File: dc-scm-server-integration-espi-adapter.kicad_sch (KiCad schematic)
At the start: 0 parts

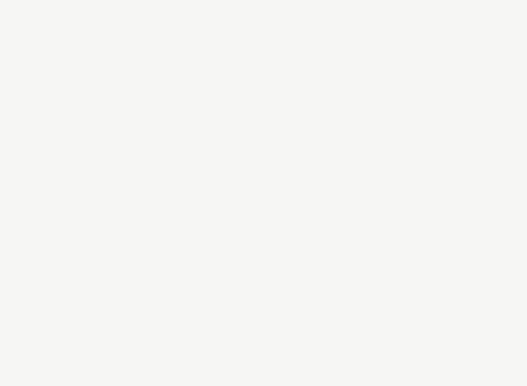
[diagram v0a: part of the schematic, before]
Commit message: [#103224] Add JTAG connector, add 2nd QSPI flash in co-layout, add Antmicro and OSH logos
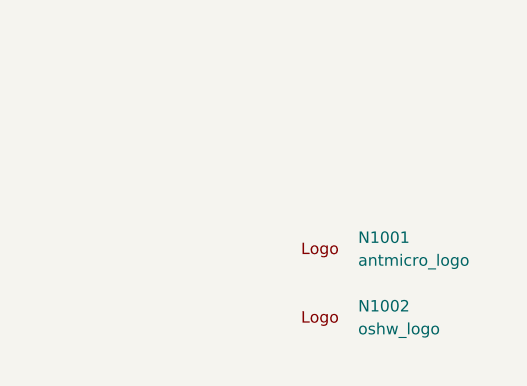
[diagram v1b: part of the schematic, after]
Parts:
- added N1001: antmicro_logo, antmicro-footprints:antmicro-logo, symbol Antmicro Symbols:antmicro_logo
- added N1002: oshw_logo, antmicro-footprints:oshw-logo, symbol Antmicro Symbols:oshw_logo

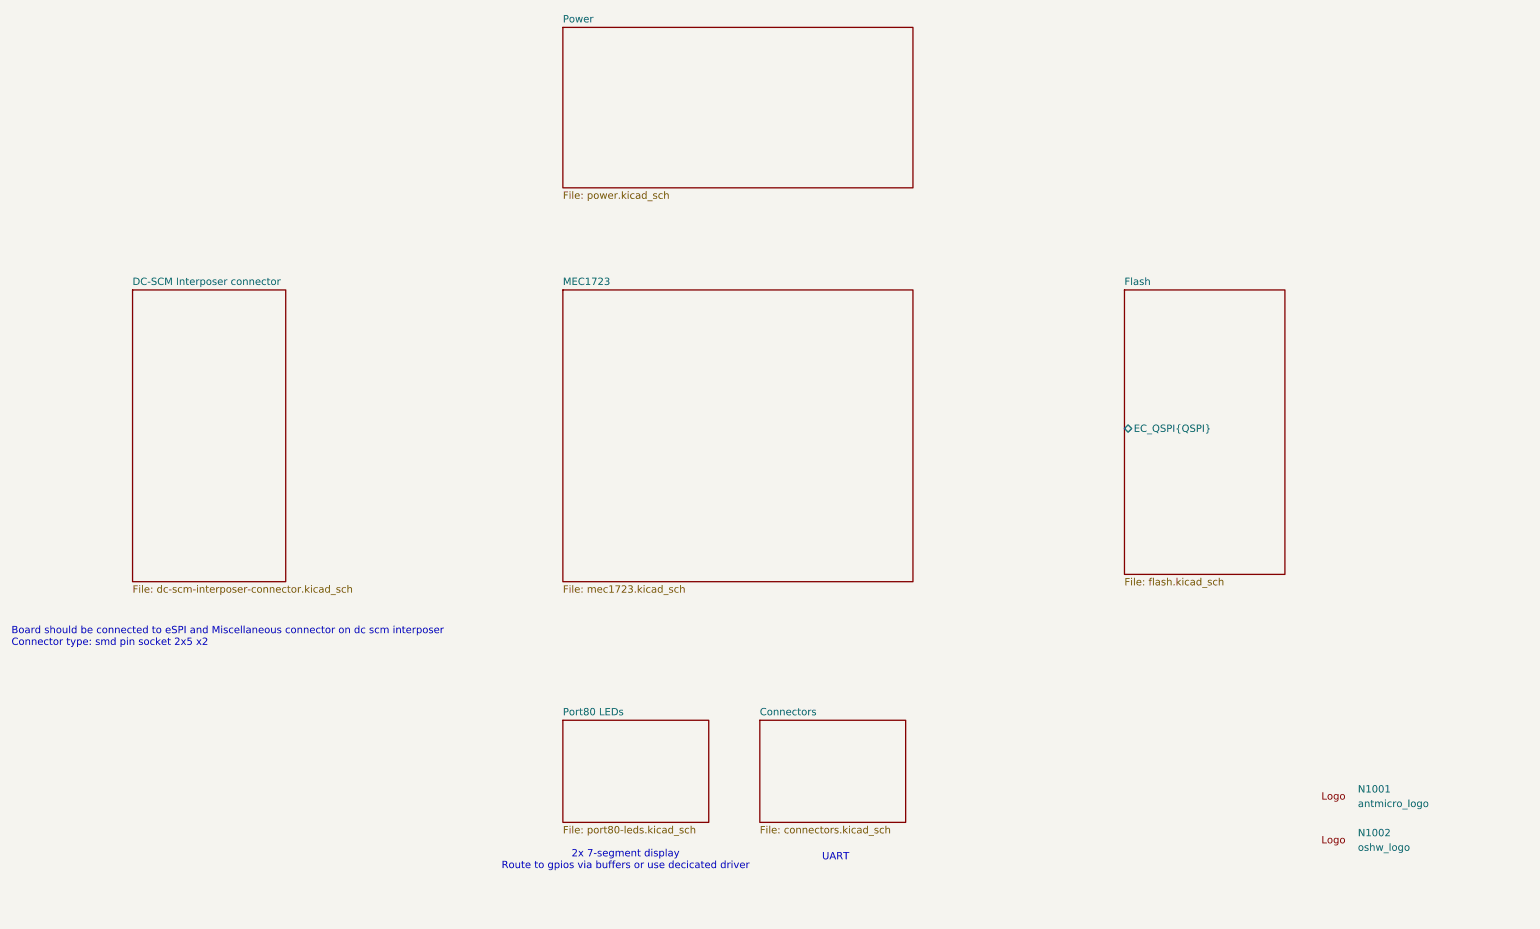
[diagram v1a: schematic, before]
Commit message: [#103224] Add MEC1723 IC, JTAG connections, eSPI connections, QSPI connections, fix typo in UART
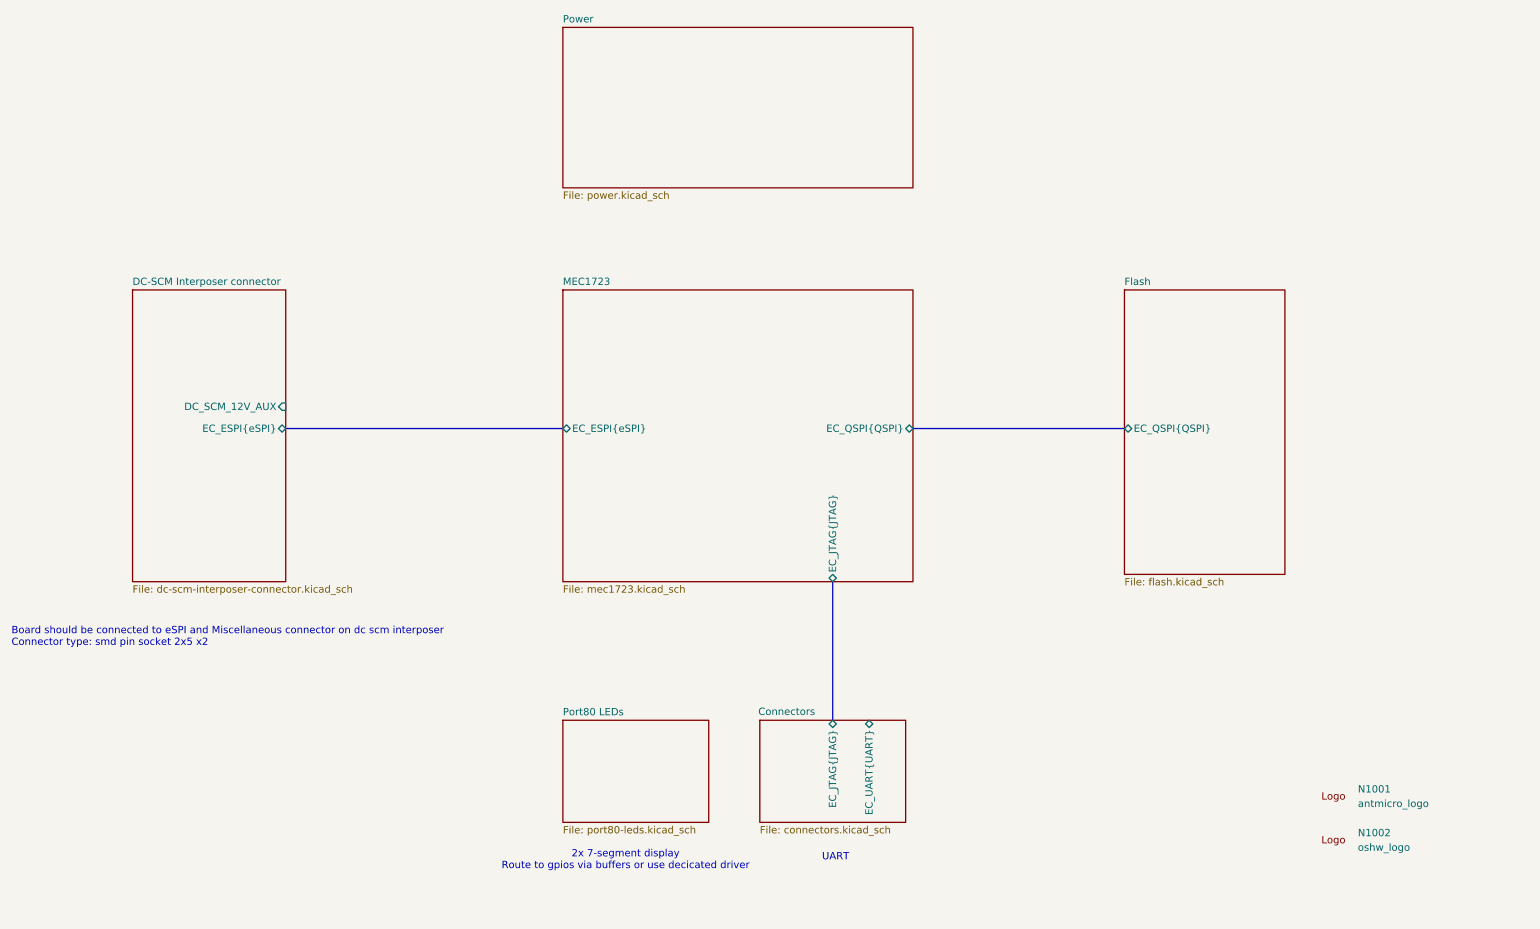
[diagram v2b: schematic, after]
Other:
- sheet Connectors ports: added EC_JTAG{JTAG}, EC_UART{UART}; removed none
- sheet DC-SCM Interposer connector ports: added DC_SCM_12V_AUX, EC_ESPI{eSPI}; removed none
- sheet MEC1723 ports: added EC_ESPI{eSPI}, EC_JTAG{JTAG}, EC_QSPI{QSPI}; removed none
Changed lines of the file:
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@@
+		)
+	)
+	(bus
+		(pts
+			(xy 179.07 90.17) (xy 215.9 90.17)
+		)
+		(stroke
+			(width 0)
+			(type default)
+		)
+	)
+	(bus
+		(pts
+			(xy 165.1 116.84) (xy 165.1 140.97)
+		)
+		(stroke
+			(width 0)
+			(type default)
+		)
+	)
+	(bus
+		(pts
+			(xy 69.85 90.17) (xy 118.11 90.17)
+		)
+		(stroke
+			(width 0)
+			(type default)
 		)
 	)
@@
 		(on_board yes)
 		(dnp no)
-		(fields_autoplaced yes)
 		(stroke
 			(width 0.1524)
@@
 		)
 		(property "Sheetname" "Connectors"
-			(at 152.4 140.2584 0)
+			(at 152.146 140.208 0)
 			(show_name no)
 			(do_not_autoplace no)
@@
 				)
 				(justify left top)
+			)
+		)
+		(pin "EC_JTAG{JTAG}" bidirectional
+			(at 165.1 140.97 90)
+			(effects
+				(font
+					(size 1.27 1.27)
+				)
+				(justify right)
+			)
+		)
+		(pin "EC_UART{UART}" bidirectional
+			(at 171.45 140.97 90)
+			(effects
+				(font
+					(size 1.27 1.27)
+				)
+				(justify right)
 			)
 		)
@@
 			)
 		)
+		(pin "EC_ESPI{eSPI}" bidirectional
+			(at 118.11 90.17 180)
+			(effects
+				(font
+					(size 1.27 1.27)
+				)
+				(justify left)
+			)
+		)
+		(pin "EC_JTAG{JTAG}" bidirectional
+			(at 165.1 116.84 270)
+			(effects
+				(font
+					(size 1.27 1.27)
+				)
+				(justify left)
+			)
+		)
+		(pin "EC_QSPI{QSPI}" bidirectional
+			(at 179.07 90.17 0)
+			(effects
+				(font
+					(size 1.27 1.27)
+				)
+				(justify right)
+			)
+		)
 		(instances
 			(project "dc-scm-server-integration-espi-adapter"
@@
 			)
 		)
+		(pin "DC_SCM_12V_AUX" input
+			(at 69.85 86.36 0)
+			(effects
+				(font
+					(size 1.27 1.27)
+				)
+				(justify right)
+			)
+		)
+		(pin "EC_ESPI{eSPI}" bidirectional
+			(at 69.85 90.17 0)
+			(effects
+				(font
+					(size 1.27 1.27)
+				)
+				(justify right)
+			)
+		)

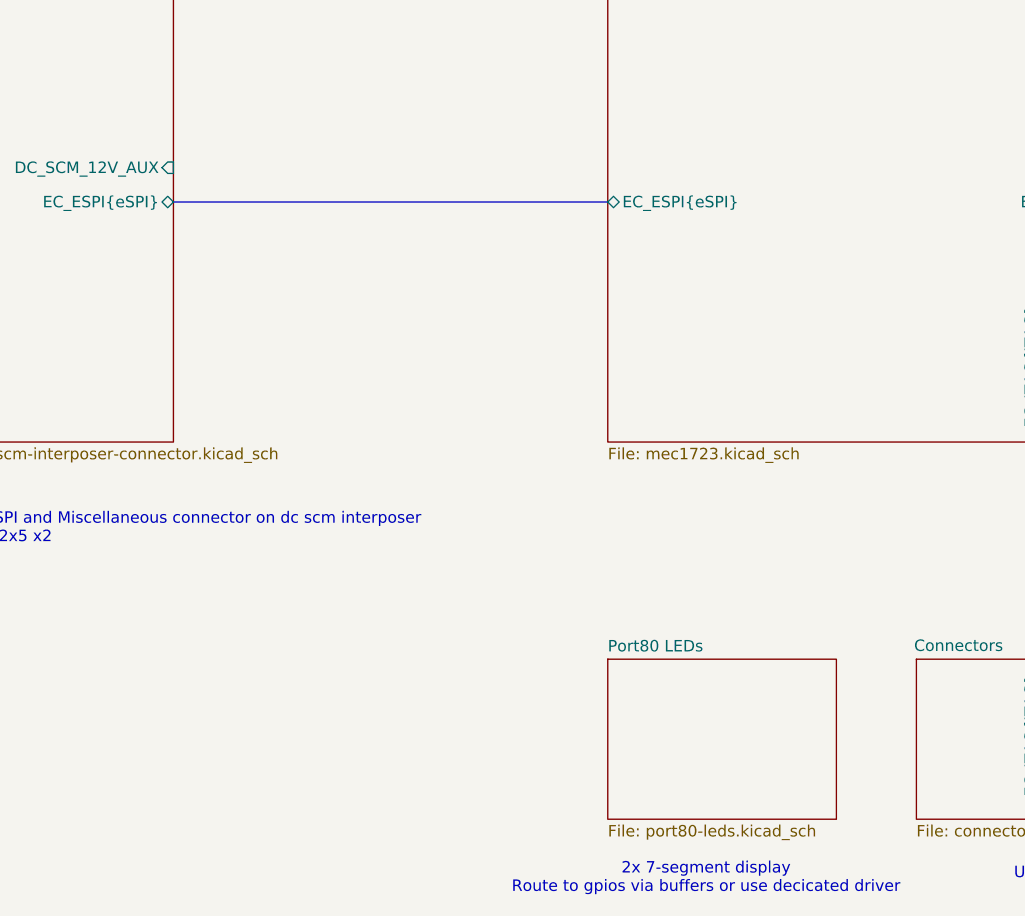
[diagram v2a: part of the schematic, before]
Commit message: [#103224] Add 7-segment display section, add battery cicruit
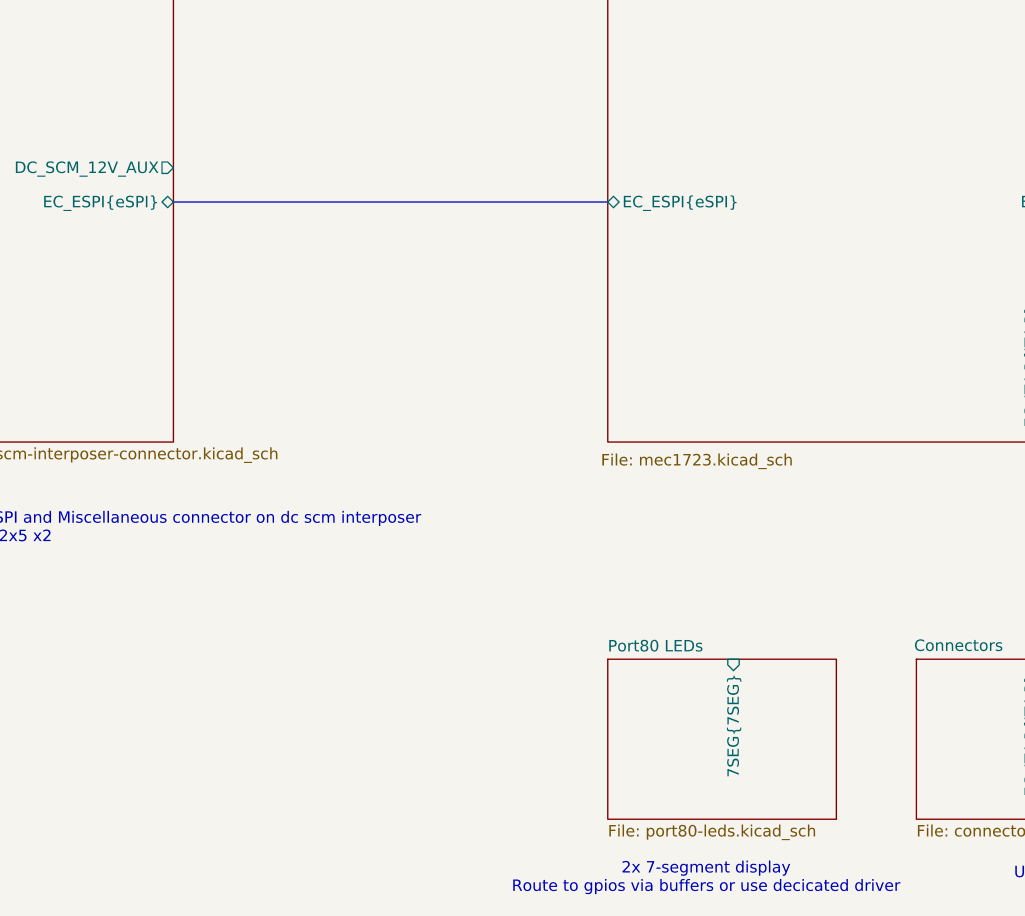
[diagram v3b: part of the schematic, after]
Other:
- sheet Port80 LEDs ports: added 7SEG{7SEG}; removed none
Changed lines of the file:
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@@
+			)
+		)
+		(pin "7SEG{7SEG}" input
+			(at 132.08 140.97 90)
+			(effects
+				(font
+					(size 1.27 1.27)
+				)
+				(justify right)
 			)
 		)
@@
 		(on_board yes)
 		(dnp no)
-		(fields_autoplaced yes)
 		(stroke
 			(width 0.1524)
@@
 		)
 		(property "Sheetfile" "mec1723.kicad_sch"
-			(at 118.11 117.4246 0)
+			(at 117.348 118.11 0)
 			(show_name no)
 			(do_not_autoplace no)
@@
 			)
 		)
-		(pin "DC_SCM_12V_AUX" input
+		(pin "DC_SCM_12V_AUX" output
 			(at 69.85 86.36 0)
 			(effects

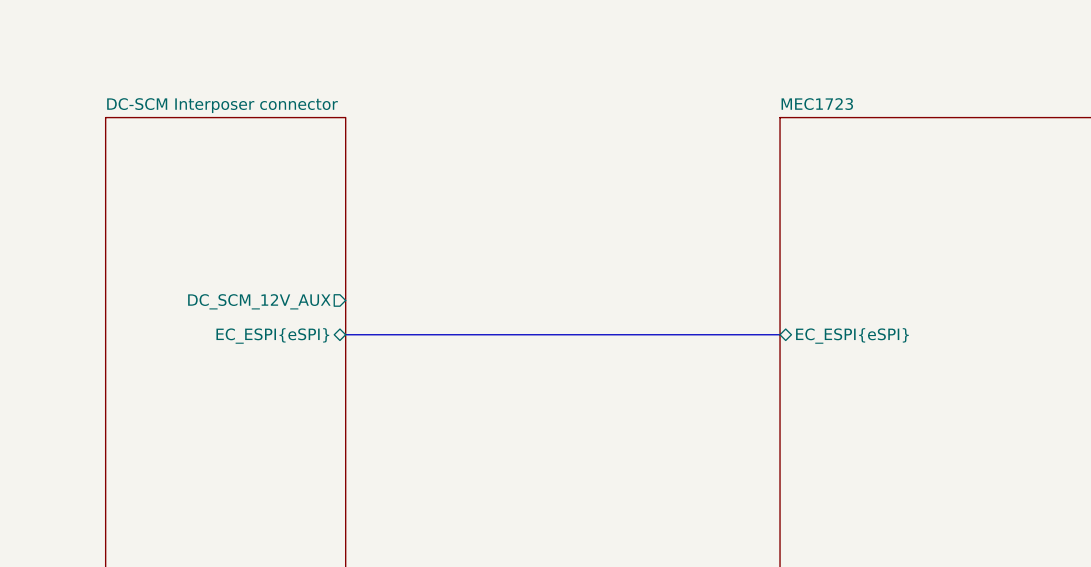
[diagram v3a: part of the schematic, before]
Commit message: [#103224] Change buffer ICs, change JTAG connector, move BSS_STRAP resistors to MEC1723 sheet
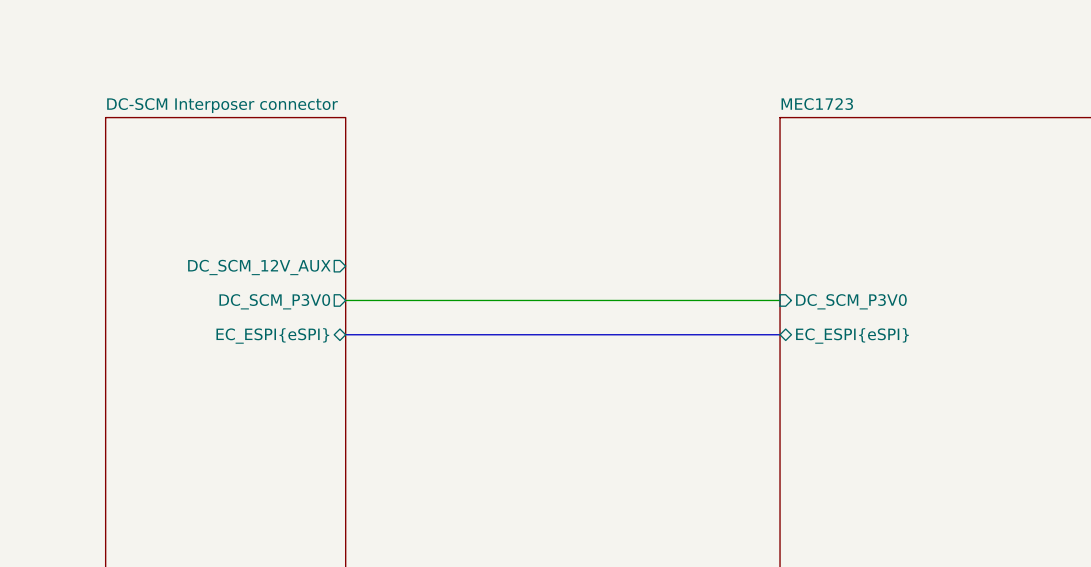
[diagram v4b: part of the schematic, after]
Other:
- sheet DC-SCM Interposer connector ports: added DC_SCM_P3V0; removed none
- sheet MEC1723 ports: added DC_SCM_P3V0; removed none
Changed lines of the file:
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@@
+		)
+	)
+	(wire
+		(pts
+			(xy 69.85 86.36) (xy 118.11 86.36)
+		)
+		(stroke
+			(width 0)
+			(type default)
 		)
 	)
@@
 			)
 		)
+		(pin "DC_SCM_P3V0" input
+			(at 118.11 86.36 180)
+			(effects
+				(font
+					(size 1.27 1.27)
+				)
+				(justify left)
+			)
+		)
 		(instances
 			(project "dc-scm-server-integration-espi-adapter"
@@
 		)
 		(pin "DC_SCM_12V_AUX" output
-			(at 69.85 86.36 0)
+			(at 69.85 82.55 0)
 			(effects
 				(font
@@
 			(effects
 				(font
+					(size 1.27 1.27)
+				)
+				(justify right)
+			)
+		)
+		(pin "DC_SCM_P3V0" output
+			(at 69.85 86.36 0)
+			(effects
+				(font

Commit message: [#103224] Route 7segment buffers, fix minor typos,add TODO list
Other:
- note added: "TODO: - Route all signals on root sheet - Change QSPI programming connector - Add the rest of strapping pins - Add testpoints do unused GPIO"
- note removed: "2x 7-segment display Route to gpios via buffers or use decicated driver"
- note removed: "Board should be connected to eSPI and Miscellaneous connector on dc scm interposer Connector type: smd pin socket 2x5 x2"
- note removed: "UART"
- company: Antmicro Ltd -> Antmicro
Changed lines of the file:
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@@
 	(title_block
 		(title "DC-SCM Server Integration eSPI Adapter HW")
-		(date "2026-08-18")
+		(date "2026-08-19")
 		(rev "1.0.0")
-		(company "Antmicro Ltd")
+		(company "Antmicro")
 		(comment 1 "www.antmicro.com")
 	)
-	(text "Board should be connected to eSPI and Miscellaneous connector on dc scm interposer\nConnector type: smd pin socket 2x5 x2"
+	(text "TODO:\n- Route all signals on root sheet\n- Change QSPI programming connector\n- Add the rest of strapping pins\n- Add testpoints do unused GPIO"
 		(exclude_from_sim no)
-		(at 22.098 126.492 0)
+		(at 23.368 154.94 0)
 		(effects
 			(font
-				(size 1.27 1.27)
+				(size 2.54 2.54)
+				(color 255 6 32 1)
 			)
 			(justify left)
 		)
 	)
-	(text "2x 7-segment display\nRoute to gpios via buffers or use decicated driver"
-		(exclude_from_sim no)
-		(at 129.032 165.354 0)
-		(effects
-			(font
-				(size 1.27 1.27)
-			)
-		)
-	)
-	(text "UART"
-		(exclude_from_sim no)
-		(at 165.608 164.846 0)
-		(effects
-			(font
-				(size 1.27 1.27)
-			)
-		)
-	)
